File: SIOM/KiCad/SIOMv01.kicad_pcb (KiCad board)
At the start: 2 copper layers, 104.1 x 120.7 mm, 139 parts, among them J101 AnaOut01, J102 P1, J103 AnaOut2, J104 I2C 5V #1, J105 TMP01, J106 TMP02, J107 TMP03, J108 I2C 5V #2, J109 TMP04, J110 TMP05, J111 AnaOut Heatpump, J112 TMP06, J113 TMP07, J114 TMP08, J115 Serial Heatpump, J116 FLOW01, J117 Boiler Heater, J118 FLOW02, J401 24V, Q301 BSS138, Q302 BSS138, Q501 BSS138, Q701 BSS138, Q702 BSS138, Q801 BSS138, Q802 BSS138, SW901 SW_Push, U201 DS2482-800, U401 LM2594M-12, U402 LM2594M-5.0, U403 LM2594M-3.3, U501 SC16IS740, U601 LM7332, U801 LM7332, U802 MAX3226, U803 SC16IS740, U804 MAX13432EESD, U901 TinyPico, Y501 7.3728MHz, Y801 7.3728MHz

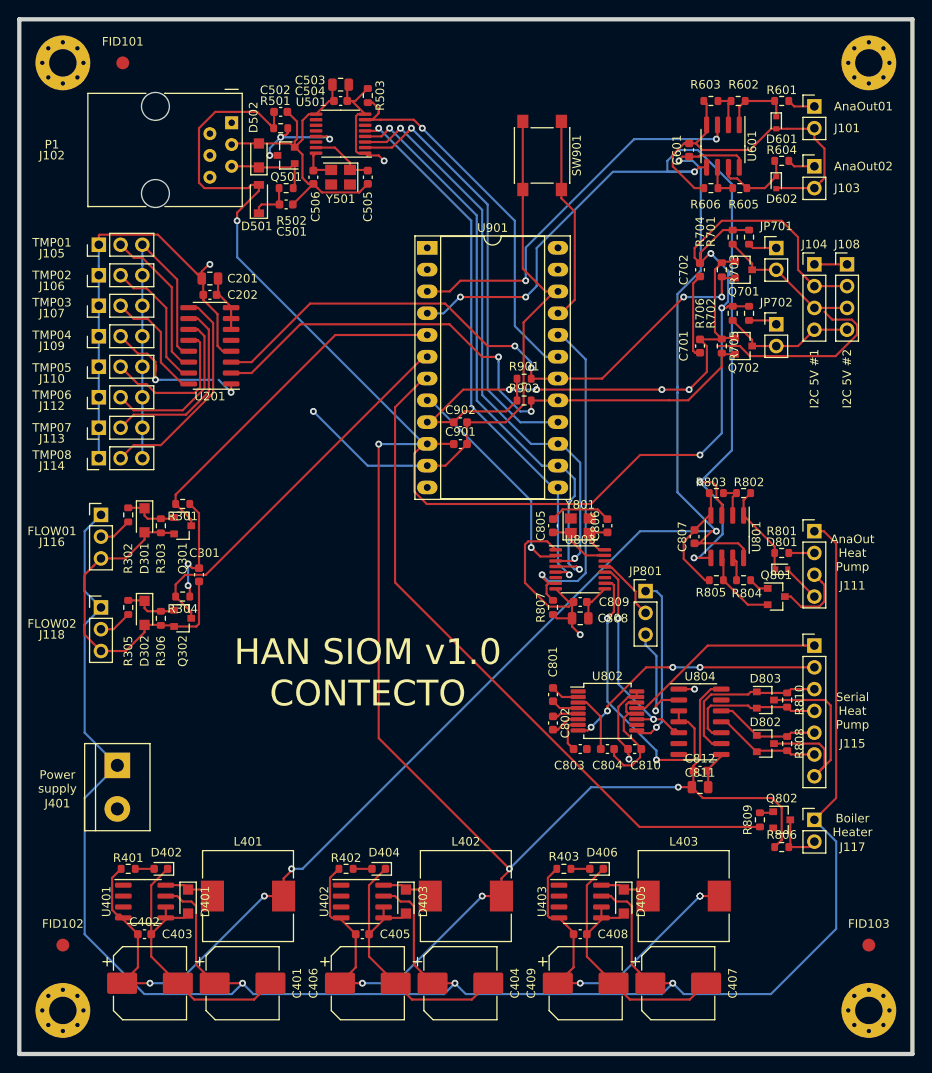
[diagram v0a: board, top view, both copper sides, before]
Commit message: KiCad files SIOM_def
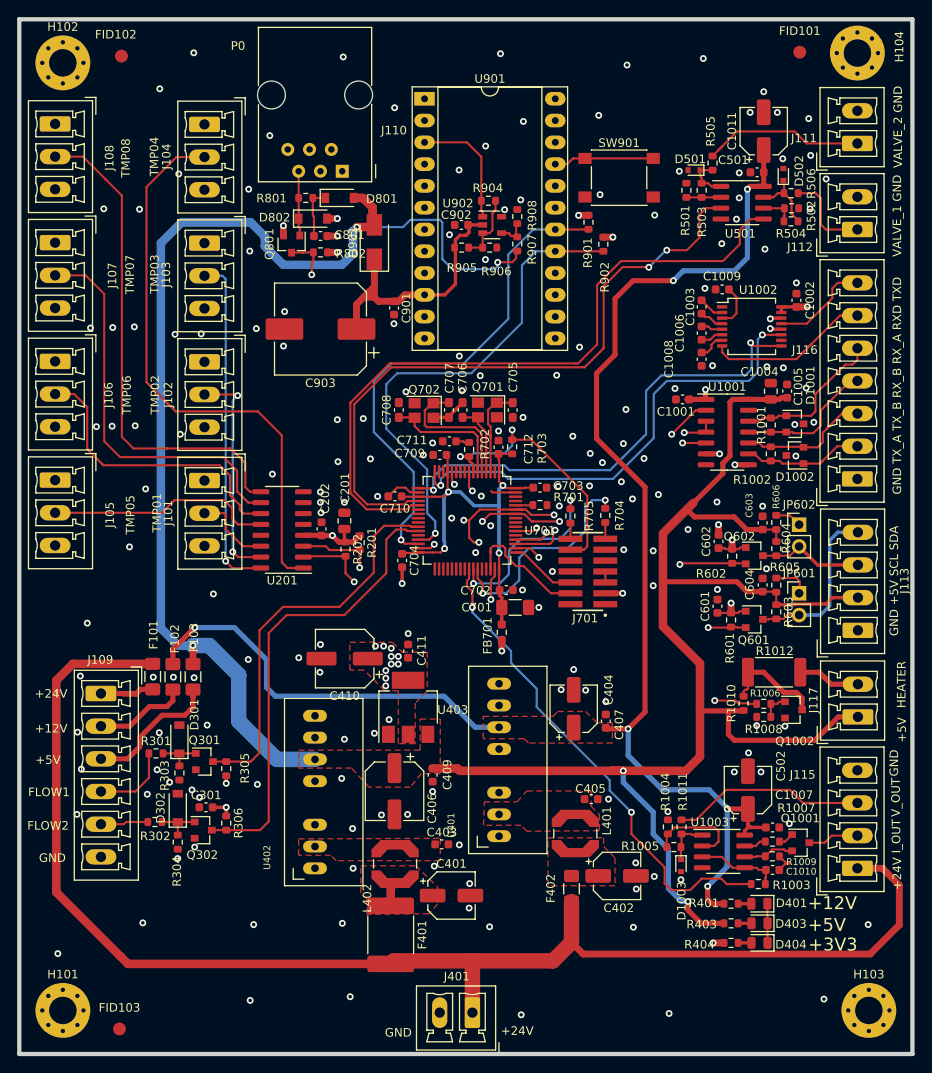
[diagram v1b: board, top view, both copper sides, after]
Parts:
- removed C408, C504, C802, C803, C804, C807, C809, C810, C812: 100n/16, Capacitor_SMD:C_0603_1608Metric
- removed C503, C808: NP, Capacitor_SMD:C_0805_2012Metric
- removed C505, C506, C805, C806: 18p, Capacitor_SMD:C_0603_1608Metric
- removed C811: 1u/16, Capacitor_SMD:C_0805_2012Metric
- removed D402, D406: Green, LED_SMD:LED_0603_1608Metric
- removed D405: PMEG4010ER, Diode_SMD:Nexperia_CFP3_SOD-123W
- removed D601, D602: DZ2S120X0L, Diode_SMD:D_SOD-523
- removed D803: SP0502BAHT, Package_TO_SOT_SMD:SOT-23
- removed J114: TMP08, Connector_PinHeader_2.54mm:PinHeader_1x03_P2.54mm_Vertical
- removed J118: FLOW02, Connector_PinHeader_2.54mm:PinHeader_1x03_P2.54mm_Vertical
- removed JP701, JP702: I2C Trm, Connector_PinHeader_2.54mm:PinHeader_1x02_P2.54mm_Vertical
- removed JP801: 232/485, Connector_PinHeader_2.54mm:PinHeader_1x03_P2.54mm_Vertical
- removed L403: 100u/1, Inductor_SMD:L_10.4x10.4_H4.8
- removed Q501, Q802: BSS138, Package_TO_SOT_SMD:SOT-23
- removed R402: 680R, Resistor_SMD:R_0603_1608Metric
- removed R706: 100k, Resistor_SMD:R_0603_1608Metric
- removed R803: 22k0, Resistor_SMD:R_0603_1608Metric
- removed R804, R809: 10k0, Resistor_SMD:R_0603_1608Metric
- removed R805: 150R, Resistor_SMD:R_0603_1608Metric
- removed R806, R807: 1k00, Resistor_SMD:R_0603_1608Metric
- removed R808, R810: 120R, Resistor_SMD:R_0603_1608Metric
- removed U601, U801: LM7332, Package_SO:SOIC-8_3.9x4.9mm_P1.27mm
- removed U802: MAX3226, Package_SO:SSOP-16_5.3x6.2mm_P0.65mm
- removed U803: SC16IS740, Package_SO:TSSOP-16_4.4x5mm_P0.65mm
- removed U804: MAX13432EESD, Package_SO:SOIC-14_3.9x8.7mm_P1.27mm
- removed Y501, Y801: 7.3728MHz, Crystal:Crystal_SMD_3225-4Pin_3.2x2.5mm
- added C1001: 100nF 50V, Capacitor_SMD:C_0603_1608Metric, F.Cu at (95.1, 104.0)
- added C1002: 100nF 50V, Capacitor_SMD:C_0603_1608Metric, F.Cu at (108.4, 92.5)
- added C1003: 100nF 50V, Capacitor_SMD:C_0603_1608Metric, F.Cu at (97.3, 93.2)
- added C1004: 1uF 16V, Capacitor_SMD:C_0805_2012Metric, F.Cu at (105.4, 103.1)
- added C1005: 100nF 50V, Capacitor_SMD:C_0603_1608Metric, F.Cu at (107.3, 103.0)
- added C1006: 100nF 50V, Capacitor_SMD:C_0603_1608Metric, F.Cu at (97.3, 96.3)
- added C1007: 100nF 50V, Capacitor_SMD:C_0603_1608Metric, F.Cu at (105.6, 153.9)
- added C1008: 100nF 50V, Capacitor_SMD:C_0603_1608Metric, F.Cu at (97.3, 99.3)
- added C1009: 100nF 50V, Capacitor_SMD:C_0603_1608Metric, F.Cu at (99.7, 91.2)
- added C1010: 100nF 50V, Capacitor_SMD:C_0603_1608Metric, F.Cu at (105.6, 158.9)
- added C1011: 10uF 50V, Capacitor_SMD:CP_Elec_5x5.3, F.Cu at (104.6, 72.7)
- added C410: 220uF 16V, Capacitor_SMD:CP_Elec_6.3x5.8, F.Cu at (55.7, 134.2)
- added C411: 100nF 50V, Capacitor_SMD:C_0603_1608Metric, F.Cu at (63.1, 133.4)
- added C602: 100nF 50V, Capacitor_SMD:C_0603_1608Metric, F.Cu at (99.3, 120.6)
- added C603: 100nF 50V, Capacitor_SMD:C_0603_1608Metric, F.Cu at (104.5, 118.4)
- added C604: 100nF 50V, Capacitor_SMD:C_0603_1608Metric, F.Cu at (104.5, 125.7)
- added C703: 100nF 50V, Capacitor_SMD:C_0603_1608Metric, F.Cu at (78.5, 114.3)
- added C704: 100nF 50V, Capacitor_SMD:C_0603_1608Metric, F.Cu at (62.4, 122.8)
- added C705: DNA, Capacitor_SMD:C_0603_1608Metric_Pad1.08x0.95mm_HandSolder, F.Cu at (75.3, 105.3)
- added C706: DNA, Capacitor_SMD:C_0603_1608Metric_Pad1.08x0.95mm_HandSolder, F.Cu at (69.5, 105.2)
- added C707: DNA, Capacitor_SMD:C_0603_1608Metric_Pad1.08x0.95mm_HandSolder, F.Cu at (67.9, 105.2)
- added C708: DNA, Capacitor_SMD:C_0603_1608Metric_Pad1.08x0.95mm_HandSolder, F.Cu at (62.0, 105.2)
- added C709: 100nF 50V, Capacitor_SMD:C_0603_1608Metric, F.Cu at (66.8, 110.5)
- added C710: 100nF 50V, Capacitor_SMD:C_0603_1608Metric, F.Cu at (61.6, 115.3)
- added C711: 100nF, Capacitor_SMD:C_0603_1608Metric, F.Cu at (67.9, 108.9)
- added C712: 100nF 50V, Capacitor_SMD:C_0603_1608Metric, F.Cu at (73.7, 109.6)
- added C903: 1000uF, Capacitor_SMD:CP_Elec_10x10.5, F.Cu at (52.9, 95.8)
- added D1001: SP0502BAHT, Package_TO_SOT_SMD:SOT-23, F.Cu at (108.2, 106.9)
- added D1002: SP0502BAHT, Package_TO_SOT_SMD:SOT-23, F.Cu at (108.2, 110.5)
- added D1003: DZ2S120X0L, Diode_SMD:D_SOD-523, F.Cu at (94.9, 158.4)
- added D901: SL13-E3/61T, Diode_SMD:D_SMA, F.Cu at (59.2, 85.7)
- added F101: 100mA, Fuse:Fuse_1206_3216Metric_Pad1.42x1.75mm_HandSolder, F.Cu at (33.3, 136.3)
- added F102: 100mA, Fuse:Fuse_1206_3216Metric_Pad1.42x1.75mm_HandSolder, F.Cu at (35.7, 136.4)
- added F103: 100mA, Fuse:Fuse_1206_3216Metric_Pad1.42x1.75mm_HandSolder, F.Cu at (38.0, 136.4)
- added F401: 1.25A Fast, Fuse:Fuse_2920_7451Metric, F.Cu at (61.1, 166.4)
- added F402: 0.1A, Fuse:Fuse_1206_3216Metric_Pad1.42x1.75mm_HandSolder, F.Cu at (82.2, 161.1)
- added FB701: 1K@100MHz, Resistor_SMD:R_0603_1608Metric_Pad0.98x0.95mm_HandSolder, F.Cu at (74.0, 131.2)
- added J701: FTSH-107-01-L-DV-K, FTSH:SAMTEC_FTSH-107-01-L-DV-K, F.Cu at (84.1, 124.1)
- added JP601: I2C Trm, Connector_PinHeader_2.54mm:PinHeader_1x02_P2.54mm_Vertical, F.Cu at (108.7, 126.6)
- added JP602: I2C Trm, Connector_PinHeader_2.54mm:PinHeader_1x02_P2.54mm_Vertical, F.Cu at (108.7, 118.6)
- added Q1001: BSS138, Package_TO_SOT_SMD:SOT-23, F.Cu at (108.9, 155.7)
- added Q1002: BSS138, Package_TO_SOT_SMD:SOT-23, F.Cu at (108.1, 140.2)
- added Q601: BSS138, Package_TO_SOT_SMD:SOT-23, F.Cu at (103.5, 129.7)
- added Q602: BSS138, Package_TO_SOT_SMD:SOT-23, F.Cu at (103.5, 122.2)
- added R1001: 120R, Resistor_SMD:R_0603_1608Metric, F.Cu at (105.4, 107.0)
- added R1002: 120R, Resistor_SMD:R_0603_1608Metric, F.Cu at (105.4, 110.4)
- added R1003: 10K, Resistor_SMD:R_0603_1608Metric, F.Cu at (103.9, 160.5)
- added R1004: 10K, Resistor_SMD:R_0603_1608Metric, F.Cu at (93.4, 153.9)
- added R1005: 22K, Resistor_SMD:R_0603_1608Metric, F.Cu at (94.1, 156.2)
- added R1006: 10K, Resistor_SMD:R_0603_1608Metric, F.Cu at (104.6, 139.5)
- added R1007: 10K, Resistor_SMD:R_0603_1608Metric, F.Cu at (105.6, 155.6)
- added R1008: 100K, Resistor_SMD:R_0603_1608Metric, F.Cu at (104.6, 141.0)
- added R1009: 150R, Resistor_SMD:R_0603_1608Metric, F.Cu at (105.6, 157.3)
- added R1010: 100K, Resistor_SMD:R_0603_1608Metric, F.Cu at (102.2, 139.4)
- added R1011: 470R, Resistor_SMD:R_0603_1608Metric, F.Cu at (95.0, 153.9)
- added R1012: 22R, Resistor_SMD:R_2512_6332Metric_Pad1.40x3.35mm_HandSolder, F.Cu at (105.8, 135.8)
- added R201: 2K2, Resistor_SMD:R_0603_1608Metric, F.Cu at (57.5, 120.7)
- added R202: 2K2, Resistor_SMD:R_0603_1608Metric, F.Cu at (55.8, 121.5)
- added R404: 270, Resistor_SMD:R_0603_1608Metric, F.Cu at (100.8, 167.4)
- added R504: 22K, Resistor_SMD:R_0603_1608Metric, F.Cu at (107.8, 83.2)
- added R505: 470R, Resistor_SMD:R_0603_1608Metric, F.Cu at (98.6, 76.5)
- added R506: 470R, Resistor_SMD:R_0603_1608Metric, F.Cu at (107.8, 80.0)
- added R904: 68K, Resistor_SMD:R_0603_1608Metric, F.Cu at (72.5, 80.8)
- added R905: 10K, Resistor_SMD:R_0603_1608Metric, F.Cu at (69.4, 86.3)
- added R906: 10K, Resistor_SMD:R_0603_1608Metric, F.Cu at (72.6, 86.3)
- added R907: 10K, Resistor_SMD:R_0603_1608Metric, F.Cu at (75.8, 85.9)
- added R908: 15K, Resistor_SMD:R_0603_1608Metric, F.Cu at (75.8, 82.7)
- added U1001: MAX13432EESD, Package_SO:SOIC-14_3.9x8.7mm_P1.27mm, F.Cu at (100.3, 107.8)
- added U1002: MAX3226, Package_SO:SSOP-16_5.3x6.2mm_P0.65mm, F.Cu at (103.2, 95.5)
- added U1003: LM7332, Package_SO:SOIC-8_3.9x4.9mm_P1.27mm, F.Cu at (99.9, 156.7)
- added U701: STM32L452RCTx, Package_QFP:LQFP-64_10x10mm_P0.5mm, F.Cu at (70.0, 118.1)
- added U902: MCP6561R, Package_TO_SOT_SMD:SOT-23-5, F.Cu at (72.9, 83.7)
- C201: value 10u/16 -> 10uF 16V
- C202, C301, C405, C601, C702, C801, C901: value 100n/16 -> 100nF 50V
- C401, C404: value 220u/35 -> 10uF 50V; footprint Capacitor_SMD:CP_Elec_8x10 -> Capacitor_SMD:CP_Elec_5x5.3
- C402, C502: value 100n/16 -> 10uF 50V; footprint Capacitor_SMD:C_0603_1608Metric -> Capacitor_SMD:CP_Elec_5x5.3
- C403: value 100u/16 -> 100nF 50V; footprint Capacitor_SMD:CP_Elec_8x10 -> Capacitor_SMD:C_0603_1608Metric
- C406: value 100u/16 -> 220uF 16V; footprint Capacitor_SMD:CP_Elec_8x10 -> Capacitor_SMD:CP_Elec_6.3x5.8
- C407: value 220u/35 -> 100nF 50V; footprint Capacitor_SMD:CP_Elec_8x10 -> Capacitor_SMD:C_0603_1608Metric
- C409: value 220u/16 -> 100nF 50V; footprint Capacitor_SMD:CP_Elec_8x10 -> Capacitor_SMD:C_0603_1608Metric
- C501: value 100n/10 -> 100nF 50V
- C701: value 100n/16 -> 10uF 16V; footprint Capacitor_SMD:C_0603_1608Metric -> Capacitor_SMD:C_1206_3216Metric_Pad1.33x1.80mm_HandSolder
- C902: value 100n/16 -> 100nF
- D301, D302: footprint Diode_SMD:Nexperia_CFP3_SOD-123W -> Diode_SMD:D_SOD-123
- D401, D403: value PMEG4010ER -> LED; footprint Diode_SMD:Nexperia_CFP3_SOD-123W -> LED_SMD:LED_0805_2012Metric
- D404: value Green -> LED; footprint LED_SMD:LED_0603_1608Metric -> LED_SMD:LED_0805_2012Metric
- D501: value 1N4148W -> DZ2S120X0L; footprint Diode_SMD:D_SOD-123 -> Diode_SMD:D_SOD-523
- D502: value PTVS5V0S1UR -> DZ2S120X0L; footprint Diode_SMD:Nexperia_CFP3_SOD-123W -> Diode_SMD:D_SOD-523
- D801: value DZ2S120X0L -> 1N4148W; footprint Diode_SMD:D_SOD-523 -> Diode_SMD:D_SOD-123
- D802: value SP0502BAHT -> PTVS5V0S1UR; footprint Package_TO_SOT_SMD:SOT-23 -> Diode_SMD:D_SOD-123
- J101: value AnaOut01 -> TMP01; footprint Connector_PinHeader_2.54mm:PinHeader_1x02_P2.54mm_Vertical -> Connector_Phoenix_MC:PhoenixContact_MCV_1,5_3-G-3.81_1x03_P3.81mm_Vertical
- J102: value P1 -> TMP02; footprint Connector_RJ:RJ12_Amphenol_54601 -> Connector_Phoenix_MC:PhoenixContact_MCV_1,5_3-G-3.81_1x03_P3.81mm_Vertical
- J103: value AnaOut2 -> TMP03; footprint Connector_PinHeader_2.54mm:PinHeader_1x02_P2.54mm_Vertical -> Connector_Phoenix_MC:PhoenixContact_MCV_1,5_3-G-3.81_1x03_P3.81mm_Vertical
- J104: value I2C 5V #1 -> TMP04; footprint Connector_PinHeader_2.54mm:PinHeader_1x04_P2.54mm_Vertical -> Connector_Phoenix_MC:PhoenixContact_MCV_1,5_3-G-3.81_1x03_P3.81mm_Vertical
- J105: value TMP01 -> TMP05; footprint Connector_PinHeader_2.54mm:PinHeader_1x03_P2.54mm_Vertical -> Connector_Phoenix_MC:PhoenixContact_MCV_1,5_3-G-3.81_1x03_P3.81mm_Vertical
- J106: value TMP02 -> TMP06; footprint Connector_PinHeader_2.54mm:PinHeader_1x03_P2.54mm_Vertical -> Connector_Phoenix_MC:PhoenixContact_MCV_1,5_3-G-3.81_1x03_P3.81mm_Vertical
- J107: value TMP03 -> TMP07; footprint Connector_PinHeader_2.54mm:PinHeader_1x03_P2.54mm_Vertical -> Connector_Phoenix_MC:PhoenixContact_MCV_1,5_3-G-3.81_1x03_P3.81mm_Vertical
- J108: value I2C 5V #2 -> TMP08; footprint Connector_PinHeader_2.54mm:PinHeader_1x04_P2.54mm_Vertical -> Connector_Phoenix_MC:PhoenixContact_MCV_1,5_3-G-3.81_1x03_P3.81mm_Vertical
- J109: value TMP04 -> Flowsensors; footprint Connector_PinHeader_2.54mm:PinHeader_1x03_P2.54mm_Vertical -> Connector_Phoenix_MC:PhoenixContact_MCV_1,5_6-G-3.81_1x06_P3.81mm_Vertical
- J110: value TMP05 -> P1; footprint Connector_PinHeader_2.54mm:PinHeader_1x03_P2.54mm_Vertical -> Connector_RJ:RJ12_Amphenol_54601
- J111: value AnaOut Heatpump -> AnaOut01; footprint Connector_PinHeader_2.54mm:PinHeader_1x04_P2.54mm_Vertical -> Connector_Phoenix_MC:PhoenixContact_MCV_1,5_2-G-3.81_1x02_P3.81mm_Vertical
- J112: value TMP06 -> AnaOut2; footprint Connector_PinHeader_2.54mm:PinHeader_1x03_P2.54mm_Vertical -> Connector_Phoenix_MC:PhoenixContact_MCV_1,5_2-G-3.81_1x02_P3.81mm_Vertical
- J113: value TMP07 -> I2C 5V #1; footprint Connector_PinHeader_2.54mm:PinHeader_1x03_P2.54mm_Vertical -> Connector_Phoenix_MC:PhoenixContact_MCV_1,5_4-G-3.81_1x04_P3.81mm_Vertical
- J115: value Serial Heatpump -> AnaOut Heatpump; footprint Connector_PinHeader_2.54mm:PinHeader_1x07_P2.54mm_Vertical -> Connector_Phoenix_MC:PhoenixContact_MCV_1,5_4-G-3.81_1x04_P3.81mm_Vertical
- J116: value FLOW01 -> Serial Heatpump; footprint Connector_PinHeader_2.54mm:PinHeader_1x03_P2.54mm_Vertical -> Connector_Phoenix_MC:PhoenixContact_MCV_1,5_7-G-3.81_1x07_P3.81mm_Vertical
- J117: footprint Connector_PinHeader_2.54mm:PinHeader_1x02_P2.54mm_Vertical -> Connector_Phoenix_MC:PhoenixContact_MCV_1,5_2-G-3.81_1x02_P3.81mm_Vertical
- J401: footprint TerminalBlock:TerminalBlock_bornier-2_P5.08mm -> Connector_Phoenix_MC:PhoenixContact_MCV_1,5_2-G-3.81_1x02_P3.81mm_Vertical
- L401: value 220u/1 -> 10uH; footprint Inductor_SMD:L_10.4x10.4_H4.8 -> Inductor_SMD:L_Coilcraft_LPS5030
- L402: value 150u/1 -> 10uH; footprint Inductor_SMD:L_10.4x10.4_H4.8 -> Inductor_SMD:L_Coilcraft_LPS5030
- Q701, Q702: value BSS138 -> DNA; footprint Package_TO_SOT_SMD:SOT-23 -> Crystal:Crystal_SMD_Abracon_ABM8G-4Pin_3.2x2.5mm
- R301, R304, R501, R502: value 1k00 -> 10K
- R302, R305: value 10k0 -> 10K
- R303, R306: value 2k20 -> 10K
- R401: value 2k20 -> 2K2
- R403: value 330R -> 680
- R503: value 1k00 -> 22K
- R601: value 470R -> 100K
- R602: value 10k0 -> 100k
- R603: value 22k0 -> 100K
- R604: value 470R -> 100k
- R605: value 10k0 -> 1K5
- R606: value 22k0 -> 1K5
- R701: value 1k50 -> 10K
- R702: value 1k50 -> 100
- R703: value 100k -> 10K
- R704, R705: value 100k -> 100R
- R801: value 470R -> 1K
- R802: value 10k0 -> 1K
- R901, R902: value 100k -> 4K7
- U401: value LM2594M-12 -> SPBW06F-12; footprint Package_SO:SOIC-8_3.9x4.9mm_P1.27mm -> FTSH:SPAN02
- U402: value LM2594M-5.0 -> SPBW06F-05; footprint Package_SO:SOIC-8_3.9x4.9mm_P1.27mm -> FTSH:SPAN02
- U403: value LM2594M-3.3 -> LM1117-3.3; footprint Package_SO:SOIC-8_3.9x4.9mm_P1.27mm -> Package_TO_SOT_SMD:SOT-223-3_TabPin2
- U501: value SC16IS740 -> LM7332; footprint Package_SO:TSSOP-16_4.4x5mm_P0.65mm -> Package_SO:SOIC-8_3.9x4.9mm_P1.27mm
- moved H104 145.1 mm to (115.5, 63.6)
- moved H101 110.5 mm to (22.9, 175.3)
- moved FID102 103.9 mm to (29.7, 64.0)
- moved C502 96.0 mm to (102.7, 149.6), turned to 90 degrees
- moved H102 94.0 mm to (22.9, 64.8)
- moved J108 93.8 mm to (22.0, 71.9), turned to 270 degrees
- moved J113 91.6 mm to (115.6, 130.9)
- moved J112 90.6 mm to (115.5, 84.2)
- moved J116 88.3 mm to (115.5, 113.3), turned to 90 degrees
- moved FID103 87.9 mm to (29.5, 177.4)
- moved J101 83.4 mm to (39.4, 113.5), turned to 270 degrees
- moved D802 80.8 mm to (52.0, 82.9)
- moved FID101 79.0 mm to (108.8, 63.5)
- moved J104 73.0 mm to (39.4, 71.9), turned to 270 degrees
- moved J103 71.7 mm to (39.4, 85.8), turned to 270 degrees
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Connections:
- net /MainCtrl/RESET renamed /TinyPico/RESET
- C401 pad 1: +24V -> Net-(C401-Pad1)
- C402 pad 1: +12V -> Net-(C402-Pad1)
- C403 pad 1: +12V -> GND
- C403 pad 2: GND -> Net-(C403-Pad2)
- C404 pad 1: +24V -> +12V
- C405 pad 1: +5V -> GND
- C405 pad 2: GND -> Net-(C405-Pad2)
- C407 pad 1: +24V -> GND
- C407 pad 2: GND -> +12V
- C409 pad 1: +3V3 -> GND
- C409 pad 2: GND -> +5V
- C501 pad 1: Net-(C501-Pad1) -> +12V
- C502 pad 1: +5V -> +12V
- C601 pad 1: +12V -> +3V3
- C701 pad 1: +3V3 -> Net-(C701-Pad1)
- C702 pad 1: +5V -> Net-(C701-Pad1)
- C801 pad 2: Net-(C801-Pad2) -> GND
- C901 pad 1: +5V -> /TinyPico/+5V_TINY_PICO
- C902 pad 1: +3V3 -> /TinyPico/+5V_TINY_PICO
- D401 pad 1: Net-(D401-Pad1) -> GND
- D401 pad 2: GND -> Net-(D401-Pad2)
- D403 pad 1: Net-(D403-Pad1) -> GND
- D403 pad 2: GND -> Net-(D403-Pad2)
- D501 pad 1: Net-(C501-Pad1) -> Net-(D501-Pad1)
- D501 pad 2: +5V -> GND
- D502 pad 1: /P1port/P1_INPUT -> Net-(D502-Pad1)
- D801 pad 1: Net-(D801-Pad1) -> Net-(C801-Pad1)
- D801 pad 2: GND -> +5V
- D802 pad 1: /ExpansionBoard/RS485_RX_A -> /P1port/P1_INPUT
- D802 pad 2: /ExpansionBoard/RS485_RX_B -> GND
- J101 pad 1: /ValveCtrl/ANA_OUT_10V_01 -> +3V3
- J101 pad 2: GND -> /TmpSensor/TMP01
- J102 pad 1: Net-(J102-Pad1) -> +3V3
- J102 pad 2: Net-(J102-Pad2) -> /TmpSensor/TMP02
- J103 pad 1: /ValveCtrl/ANA_OUT_10V_02 -> +3V3
- J103 pad 2: GND -> /TmpSensor/TMP03
- J104 pad 1: GND -> +3V3
- J104 pad 2: +5V -> /TmpSensor/TMP04
- J104 pad 3: /I2CInterface/SDA_5V -> GND
- J105 pad 2: /TmpSensor/TMP01 -> /TmpSensor/TMP05
- J106 pad 2: /TmpSensor/TMP02 -> /TmpSensor/TMP06
- J107 pad 2: /TmpSensor/TMP03 -> /TmpSensor/TMP07
- J108 pad 1: GND -> +3V3
- J108 pad 2: +5V -> /TmpSensor/TMP08
- J108 pad 3: /I2CInterface/SDA_5V -> GND
- J109 pad 1: +3V3 -> Net-(F101-Pad1)
- J109 pad 2: /TmpSensor/TMP04 -> Net-(F102-Pad1)
- J109 pad 3: GND -> Net-(F103-Pad1)
- J110 pad 1: +3V3 -> Net-(J110-Pad1)
- J110 pad 2: /TmpSensor/TMP05 -> Net-(J110-Pad2)
- J111 pad 1: +24V -> /ValveCtrl/ANA_OUT_10V_01
- J111 pad 2: /ExpansionBoard/V_OUT -> GND
- J112 pad 1: +3V3 -> /ValveCtrl/ANA_OUT_10V_02
- J112 pad 2: /TmpSensor/TMP06 -> GND
- J113 pad 1: +3V3 -> GND
- J113 pad 2: /TmpSensor/TMP07 -> +5V
- J113 pad 3: GND -> /I2CInterface/SCL_5V
- J115 pad 1: /ExpansionBoard/TXD -> +24V
- J115 pad 2: /ExpansionBoard/RXD -> /ExpansionBoard/I_OUT
- J115 pad 3: /ExpansionBoard/RS485_TX_A -> /ExpansionBoard/V_OUT
- J115 pad 4: /ExpansionBoard/RS485_TX_B -> GND
- J116 pad 1: +24V -> GND
- J116 pad 2: /FlowInput/FLOW_01 -> /ExpansionBoard/RS485_TX_A
- J116 pad 3: GND -> /ExpansionBoard/RS485_TX_B
- J117 pad 1: +24V -> +5V
- L401 pad 1: Net-(D401-Pad1) -> Net-(C402-Pad1)
- L401 pad 2: +12V -> Net-(C405-Pad2)
- L402 pad 1: Net-(D403-Pad1) -> Net-(C401-Pad1)
- L402 pad 2: +5V -> Net-(C403-Pad2)
- Q301 pad 3: /FlowInput/FLOW_IN_01 -> /MainCtrl/EXTI0_FREQ_CALC
- Q302 pad 3: /FlowInput/FLOW_IN_02 -> /MainCtrl/EXTI1_FREQ_CALC
- Q701 pad 1: +3V3 -> Net-(C705-Pad1)
- Q701 pad 2: /I2CInterface/SDA_AUX -> GND
- Q701 pad 3: /I2CInterface/SDA_5V -> Net-(C706-Pad1)
- Q702 pad 1: +3V3 -> Net-(C707-Pad1)
- Q702 pad 2: /I2CInterface/SCL_AUX -> GND
- Q702 pad 3: /I2CInterface/SCL_5V -> Net-(C708-Pad1)
- Q801 pad 1: Net-(Q801-Pad1) -> /P1port/P1_INPUT
- Q801 pad 2: Net-(Q801-Pad2) -> GND
- Q801 pad 3: /ExpansionBoard/I_OUT -> /MainCtrl/LPUART1_RX_P1
- R301 pad 1: +3V3 -> /FlowInput/FLOW_01
- R301 pad 2: /FlowInput/FLOW_IN_01 -> Net-(D301-Pad1)
- R302 pad 1: /FlowInput/FLOW_01 -> /FlowInput/FLOW_02
- R302 pad 2: Net-(D301-Pad1) -> Net-(D302-Pad1)
- R304 pad 1: +3V3 -> Net-(D302-Pad1)
- R304 pad 2: /FlowInput/FLOW_IN_02 -> GND
- R305 pad 1: /FlowInput/FLOW_02 -> +3V3
- R305 pad 2: Net-(D302-Pad1) -> /MainCtrl/EXTI0_FREQ_CALC
- R306 pad 1: Net-(D302-Pad1) -> +3V3
- R306 pad 2: GND -> /MainCtrl/EXTI1_FREQ_CALC
- R401 pad 2: Net-(D402-Pad2) -> Net-(D401-Pad2)
- R403 pad 1: +3V3 -> +5V
- R403 pad 2: Net-(D406-Pad2) -> Net-(D403-Pad2)
- R501 pad 1: +5V -> Net-(R501-Pad1)
- R501 pad 2: Net-(Q501-Pad3) -> GND
- R502 pad 1: Net-(C501-Pad1) -> Net-(R502-Pad1)
- R502 pad 2: /P1port/P1_INPUT -> GND
- R503 pad 1: +3V3 -> Net-(D501-Pad1)
- R503 pad 2: /MainCtrl/INT_P1 -> Net-(R501-Pad1)
- R601 pad 1: /ValveCtrl/ANA_OUT_10V_01 -> +3V3
- R601 pad 2: Net-(D601-Pad1) -> /MainCtrl/I2C1_SDA_TEMP_SENSORS
- R602 pad 1: Net-(D601-Pad1) -> +3V3
- R602 pad 2: Net-(R602-Pad2) -> /MainCtrl/I2C1_SCL_TEMP_SENSORS
- R603 pad 1: Net-(R602-Pad2) -> +5V
- R603 pad 2: GND -> /I2CInterface/SDA_5V
- R604 pad 1: /ValveCtrl/ANA_OUT_10V_02 -> +5V
- R604 pad 2: Net-(D602-Pad1) -> /I2CInterface/SCL_5V
- R605 pad 1: Net-(D602-Pad1) -> +5V
- R605 pad 2: Net-(R605-Pad2) -> Net-(JP601-Pad1)
- R606 pad 1: Net-(R605-Pad2) -> +5V
- R606 pad 2: GND -> Net-(JP602-Pad1)
- R701 pad 1: +5V -> Net-(R701-Pad1)
- R701 pad 2: Net-(JP701-Pad1) -> GND
- R702 pad 1: +5V -> Net-(C711-Pad1)
- R702 pad 2: Net-(JP702-Pad1) -> /MainCtrl/NRESET
- R703 pad 1: +3V3 -> /MainCtrl/NRESET
- R703 pad 2: /I2CInterface/SDA_AUX -> Net-(C701-Pad1)
- R704 pad 1: +5V -> /MainCtrl/USART1_RX_DEBUG
- R704 pad 2: /I2CInterface/SDA_5V -> Net-(J701-Pad13)
- R705 pad 1: +3V3 -> /MainCtrl/USART1_TX_DEBUG
- R705 pad 2: /I2CInterface/SCL_AUX -> Net-(J701-Pad14)
- R801 pad 1: /ExpansionBoard/V_OUT -> Net-(C801-Pad1)
- R801 pad 2: Net-(D801-Pad1) -> /P1port/P1_INPUT
- R802 pad 1: Net-(D801-Pad1) -> +3V3
- R802 pad 2: Net-(R802-Pad2) -> /MainCtrl/LPUART1_RX_P1
- R901 pad 2: /I2CInterface/SDA_AUX -> /MainCtrl/I2C2_SDA_EEPROM
- R902 pad 2: /I2CInterface/SCL_AUX -> /MainCtrl/I2C2_SCL_EEPROM
- U201 pad 2: /I2CInterface/SCL_AUX -> /MainCtrl/I2C1_SCL_TEMP_SENSORS
- U201 pad 3: /I2CInterface/SDA_AUX -> /MainCtrl/I2C1_SDA_TEMP_SENSORS
- U401 pad 1: Net-(U401-Pad1) -> GND
- U401 pad 2: Net-(U401-Pad2) -> Net-(C405-Pad2)
- U401 pad 3: Net-(U401-Pad3) -> (no net)
- U401 pad 5: GND -> (no net)
- U401 pad 6: GND -> +12V
- U401 pad 7: +24V -> GND
- U401 pad 8: Net-(D401-Pad1) -> (no net)
- U402 pad 1: Net-(U402-Pad1) -> GND
- U402 pad 2: Net-(U402-Pad2) -> Net-(C403-Pad2)
- U402 pad 3: Net-(U402-Pad3) -> (no net)
- U402 pad 5: GND -> (no net)
- U402 pad 6: GND -> +5V
- U402 pad 7: +24V -> GND
- U402 pad 8: Net-(D403-Pad1) -> (no net)
- U403 pad 1: Net-(U403-Pad1) -> GND
- U403 pad 2: Net-(U403-Pad2) -> +3V3
- U403 pad 3: Net-(U403-Pad3) -> +5V
- U501 pad 1: +3V3 -> Net-(D501-Pad1)
- U501 pad 2: /MainCtrl/SPI_CS_P1 -> Net-(R501-Pad1)
- U501 pad 3: /ExpansionBoard/SPI_MOSI -> /MainCtrl/DAC1_OUT1_VALVE_1
- U501 pad 4: /ExpansionBoard/SPI_MISO -> GND
- U501 pad 5: /ExpansionBoard/SPI_SCLK -> /MainCtrl/DAC1_OUT2_VALVE_2
- U501 pad 6: Net-(U501-Pad6) -> Net-(R502-Pad1)
- U501 pad 7: /MainCtrl/INT_P1 -> Net-(D502-Pad1)
- U501 pad 8: +3V3 -> +12V
- U901 pad 10: +5V -> /TinyPico/+5V_TINY_PICO
- U901 pad 13: /ExpansionBoard/SPI_SCLK -> Net-(U901-Pad13)
- U901 pad 14: /ExpansionBoard/SPI_MISO -> Net-(U901-Pad14)
- U901 pad 15: /ExpansionBoard/SPI_MOSI -> Net-(U901-Pad15)
- U901 pad 16: /MainCtrl/SPI_CS_P1 -> Net-(U901-Pad16)
- U901 pad 17: /I2CInterface/SCL_AUX -> /MainCtrl/I2C2_SCL_EEPROM
- U901 pad 18: /I2CInterface/SDA_AUX -> /MainCtrl/I2C2_SDA_EEPROM
- U901 pad 19: /MainCtrl/INT_P1 -> Net-(U901-Pad19)
- U901 pad 20: /ExpansionBoard/INT_HP -> Net-(U901-Pad20)
- U901 pad 3: /MainCtrl/ANA_OUT_01 -> /TinyPico/DI_POWER_DROP
- U901 pad 4: /MainCtrl/ANA_OUT_02 -> Net-(U901-Pad4)
- U901 pad 5: /FlowInput/FLOW_IN_01 -> Net-(U901-Pad5)
- U901 pad 6: /FlowInput/FLOW_IN_02 -> Net-(U901-Pad6)
- U901 pad 7: /ExpansionBoard/BOILER -> Net-(U901-Pad7)
- U901 pad 8: /ExpansionBoard/SPI_CS_HP -> Net-(U901-Pad8)
- U901 pad 9: +3V3 -> Net-(U901-Pad9)
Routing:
- net GND: track 429.5 -> 40.1 mm, vias 1 -> 185
- net +3V3: track 227.6 -> 36.4 mm, vias 14 -> 24
- net /MainCtrl/ANA_OUT_02: track 112.1 -> 0.00 mm, vias 5 -> 0
- net +24V: track 251.6 -> 162.6 mm, vias 3 -> 0
- net /MainCtrl/DAC1_OUT2_VALVE_2: track 0.00 -> 82.6 mm
- net /MainCtrl/I2C1_SDA_TEMP_SENSORS: track 0.00 -> 76.8 mm, vias 0 -> 5
- net /MainCtrl/DAC1_OUT1_VALVE_1: track 0.00 -> 76.5 mm, vias 0 -> 2
- net /I2CInterface/SDA_AUX: track 72.7 -> 0.00 mm, vias 4 -> 0
- net /I2CInterface/SCL_AUX: track 72.1 -> 0.00 mm, vias 2 -> 0
- net /MainCtrl/I2C1_SCL_TEMP_SENSORS: track 0.00 -> 70.9 mm, vias 0 -> 4
- net /ExpansionBoard/SPI_MISO: track 69.0 -> 0.00 mm, vias 2 -> 0
- net /ExpansionBoard/SPI_MOSI: track 68.3 -> 0.00 mm, vias 2 -> 0
- net /ExpansionBoard/SPI_SCLK: track 65.1 -> 0.00 mm, vias 2 -> 0
- net /MainCtrl/I2C2_SDA_EEPROM: track 0.00 -> 60.0 mm, vias 0 -> 1
- net /MainCtrl/I2C2_SCL_EEPROM: track 0.00 -> 57.7 mm, vias 0 -> 1
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- added copper zone on F.Cu, net +12V
- added copper zone on F.Cu, net +3V3
- added copper zone on In1.Cu, net +3V3
- added copper zone on F.Cu, net +5V
- added copper zone on B.Cu, net GND
- added copper zone on In2.Cu, net GND
- added copper zone on F.Cu, net Net-(C401-Pad1)
- added copper zone on F.Cu, net Net-(C402-Pad1)
- added copper zone on F.Cu, net Net-(C403-Pad2)
- added copper zone on F.Cu, net Net-(C405-Pad2)
- removed copper zone on B.Cu, net +3V3
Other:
- copper layers 2 -> 4
- board text added: "+12V"
- board text added: "+24V"
- board text added: "+3V3"
- board text added: "+5V"
- board text added: "FLOW1"
- board text added: "FLOW2"
- board text added: "GND"
- board text added: "GND +5V SCL SDA"
- board text added: "GND TX_A TX_B RX_B RX_A RXD TXD"
- board text added: "HEATER"
- board text added: "I_OUT"
- board text added: "P0"
- board text added: "VALVE_1 GND"
- board text added: "VALVE_2 GND"
- board text added: "V_OUT"
- board text removed: "AnaOut Heat Pump"
- board text removed: "AnaOut01"
- board text removed: "AnaOut02"
- board text removed: "Boiler Heater"
- board text removed: "FLOW01"
- board text removed: "FLOW02"
- board text removed: "HAN SIOM v1.0 CONTECTO"
- board text removed: "I2C 5V #1"
- board text removed: "I2C 5V #2"
- board text removed: "P1"
- board text removed: "Power supply"
- board text removed: "Serial Heat Pump"
